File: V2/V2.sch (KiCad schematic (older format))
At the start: 197 parts

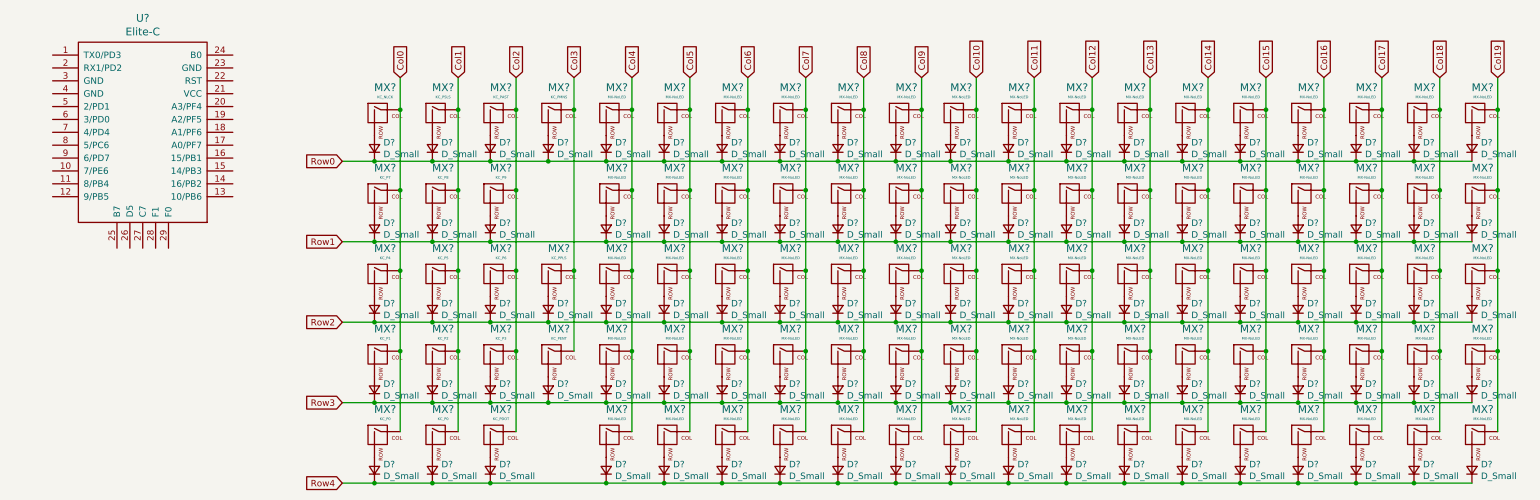
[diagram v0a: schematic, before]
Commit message: Assigned Footprints
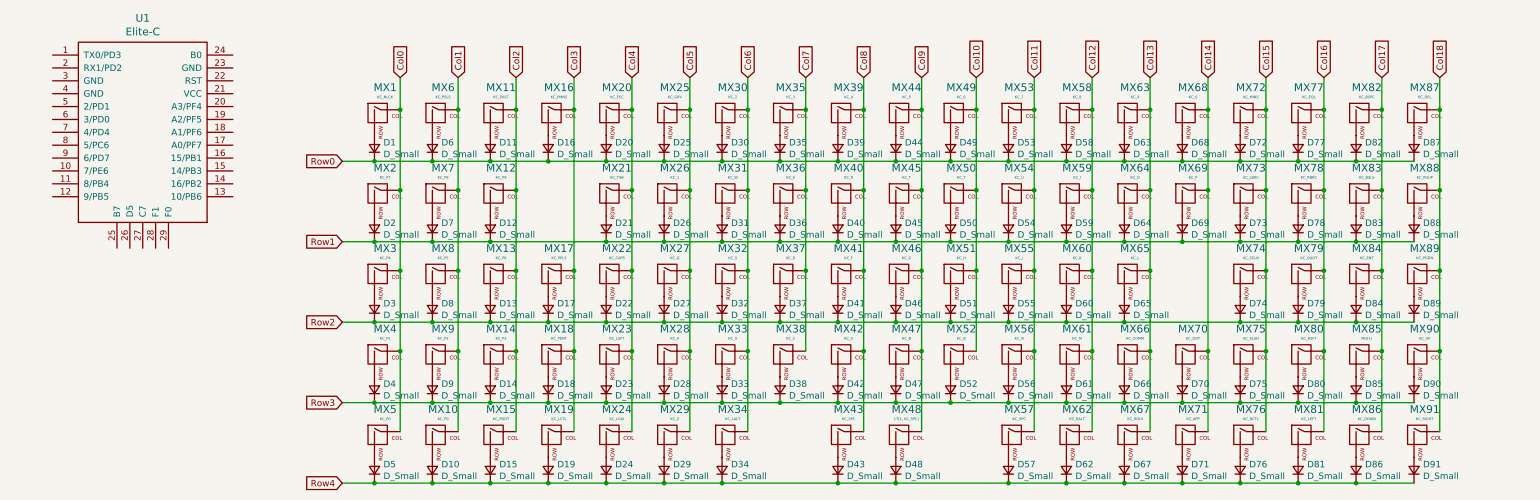
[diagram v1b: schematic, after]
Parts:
- removed D? (x8): D_Small, symbol Device:D_Small
- removed MX? (x8): MX-NoLED, symbol MX_Alps_Hybrid:MX-NoLED
- added D19: D_Small, Diode_SMD:D_SOD-123, symbol Device:D_Small
- added MX19: KC_LCTL, MX_Alps_Hybrid:MXOnly-1.25U-Hotswap, symbol MX_Alps_Hybrid:MX-NoLED
- D1, D10, D11, D12, D13, D14, D15, D16, D17, D18, D2, D20, D21, D22, D23, D24, D25, D26, D27, D28, D29, D3, D30, D31, D32, D33, D34, D35, D36, D37, D38, D39, D4, D40, D41, D42, D43, D44, D45, D46, D47, D48, D49, D5, D50, D51, D52, D53, D54, D55, D56, D57, D58, D59, D6, D60, D61, D62, D63, D64, D65, D66, D67, D68, D69, D7, D70, D71, D72, D73, D74, D75, D76, D77, D78, D79, D8, D80, D81, D82, D83, D84, D85, D86, D87, D88, D89, D9, D90, D91: renamed from D?; footprint (none) -> Diode_SMD:D_SOD-123
- MX1, MX10, MX11, MX12, MX13, MX14, MX15, MX16, MX2, MX3, MX4, MX5, MX6, MX7, MX8, MX9: renamed from MX?; footprint (none) -> MX_Alps_Hybrid:MXOnly-1U-Hotswap
- MX17, MX18: renamed from MX?; footprint (none) -> MX_Alps_Hybrid:MXOnly-2U-Hotswap
- MX20: renamed from MX?; value MX-NoLED -> KC_ESC; footprint (none) -> MX_Alps_Hybrid:MXOnly-1U-Hotswap
- MX21: renamed from MX?; value MX-NoLED -> KC_TAB; footprint (none) -> MX_Alps_Hybrid:MXOnly-1.5U-Hotswap
- MX22: renamed from MX?; value MX-NoLED -> KC_CAPS; footprint (none) -> MX_Alps_Hybrid:MXOnly-1.75U-Hotswap
- MX23: renamed from MX?; value MX-NoLED -> KC_LSFT; footprint (none) -> MX_Alps_Hybrid:MXOnly-2.25U-Hotswap
- MX24: renamed from MX?; value MX-NoLED -> KC_LGUI; footprint (none) -> MX_Alps_Hybrid:MXOnly-1.25U-Hotswap
- MX25: renamed from MX?; value MX-NoLED -> KC_GRV; footprint (none) -> MX_Alps_Hybrid:MXOnly-1U-Hotswap
- MX26: renamed from MX?; value MX-NoLED -> KC_1; footprint (none) -> MX_Alps_Hybrid:MXOnly-1U-Hotswap
- MX27: renamed from MX?; value MX-NoLED -> KC_Q; footprint (none) -> MX_Alps_Hybrid:MXOnly-1U-Hotswap
- MX28: renamed from MX?; value MX-NoLED -> KC_A; footprint (none) -> MX_Alps_Hybrid:MXOnly-1U-Hotswap
- MX29: renamed from MX?; value MX-NoLED -> KC_Z; footprint (none) -> MX_Alps_Hybrid:MXOnly-1U-Hotswap
- MX30: renamed from MX?; value MX-NoLED -> KC_2; footprint (none) -> MX_Alps_Hybrid:MXOnly-1U-Hotswap
- MX31: renamed from MX?; value MX-NoLED -> KC_W; footprint (none) -> MX_Alps_Hybrid:MXOnly-1U-Hotswap
- MX32: renamed from MX?; value MX-NoLED -> KC_S; footprint (none) -> MX_Alps_Hybrid:MXOnly-1U-Hotswap
- MX33: renamed from MX?; value MX-NoLED -> KC_X; footprint (none) -> MX_Alps_Hybrid:MXOnly-1U-Hotswap
- MX34: renamed from MX?; value MX-NoLED -> KC_LALT; footprint (none) -> MX_Alps_Hybrid:MXOnly-1.25U-Hotswap
- MX35: renamed from MX?; value MX-NoLED -> KC_3; footprint (none) -> MX_Alps_Hybrid:MXOnly-1U-Hotswap
- MX36: renamed from MX?; value MX-NoLED -> KC_E; footprint (none) -> MX_Alps_Hybrid:MXOnly-1U-Hotswap
- MX37: renamed from MX?; value MX-NoLED -> KC_D; footprint (none) -> MX_Alps_Hybrid:MXOnly-1U-Hotswap
- MX38: renamed from MX?; value MX-NoLED -> KC_C; footprint (none) -> MX_Alps_Hybrid:MXOnly-1U-Hotswap
- MX39: renamed from MX?; value MX-NoLED -> KC_4; footprint (none) -> MX_Alps_Hybrid:MXOnly-1U-Hotswap
- MX40: renamed from MX?; value MX-NoLED -> KC_R; footprint (none) -> MX_Alps_Hybrid:MXOnly-1U-Hotswap
- MX41: renamed from MX?; value MX-NoLED -> KC_F; footprint (none) -> MX_Alps_Hybrid:MXOnly-1U-Hotswap
- MX42: renamed from MX?; value MX-NoLED -> KC_V; footprint (none) -> MX_Alps_Hybrid:MXOnly-1U-Hotswap
- MX43: renamed from MX?; value MX-NoLED -> KC_SPC; footprint (none) -> MX_Alps_Hybrid:MXOnly-2.25U-Hotswap-ReversedStabilizers
- MX44: renamed from MX?; value MX-NoLED -> KC_5; footprint (none) -> MX_Alps_Hybrid:MXOnly-1U-Hotswap
- MX45: renamed from MX?; value MX-NoLED -> KC_T; footprint (none) -> MX_Alps_Hybrid:MXOnly-1U-Hotswap
- MX46: renamed from MX?; value MX-NoLED -> KC_G; footprint (none) -> MX_Alps_Hybrid:MXOnly-1U-Hotswap
- MX47, MX52: renamed from MX?; value MX-NoLED -> KC_B; footprint (none) -> MX_Alps_Hybrid:MXOnly-1U-Hotswap
- MX48: renamed from MX?; value MX-NoLED -> LT(1, KC_SPC); footprint (none) -> MX_Alps_Hybrid:MXOnly-1U-Hotswap
- MX49: renamed from MX?; value MX-NoLED -> KC_6; footprint (none) -> MX_Alps_Hybrid:MXOnly-1U-Hotswap
- MX50: renamed from MX?; value MX-NoLED -> KC_Y; footprint (none) -> MX_Alps_Hybrid:MXOnly-1U-Hotswap
- MX51: renamed from MX?; value MX-NoLED -> KC_H; footprint (none) -> MX_Alps_Hybrid:MXOnly-1U-Hotswap
- MX53: renamed from MX?; value MX-NoLED -> KC_7; footprint (none) -> MX_Alps_Hybrid:MXOnly-1U-Hotswap
- MX54: renamed from MX?; value MX-NoLED -> KC_U; footprint (none) -> MX_Alps_Hybrid:MXOnly-1U-Hotswap
- MX55: renamed from MX?; value MX-NoLED -> KC_J; footprint (none) -> MX_Alps_Hybrid:MXOnly-1U-Hotswap
- MX56: renamed from MX?; value MX-NoLED -> KC_N; footprint (none) -> MX_Alps_Hybrid:MXOnly-1U-Hotswap
- MX57: renamed from MX?; value MX-NoLED -> KC_SPC; footprint (none) -> MX_Alps_Hybrid:MXOnly-2.75U-Hotswap-ReversedStabilizers
- MX58: renamed from MX?; value MX-NoLED -> KC_8; footprint (none) -> MX_Alps_Hybrid:MXOnly-1U-Hotswap
- MX59: renamed from MX?; value MX-NoLED -> KC_I; footprint (none) -> MX_Alps_Hybrid:MXOnly-1U-Hotswap
- MX60: renamed from MX?; value MX-NoLED -> KC_K; footprint (none) -> MX_Alps_Hybrid:MXOnly-1U-Hotswap
- MX61: renamed from MX?; value MX-NoLED -> KC_M; footprint (none) -> MX_Alps_Hybrid:MXOnly-1U-Hotswap
- MX62: renamed from MX?; value MX-NoLED -> KC_RALT; footprint (none) -> MX_Alps_Hybrid:MXOnly-1.25U-Hotswap
- MX63: renamed from MX?; value MX-NoLED -> KC_9; footprint (none) -> MX_Alps_Hybrid:MXOnly-1U-Hotswap
- MX64: renamed from MX?; value MX-NoLED -> KC_O; footprint (none) -> MX_Alps_Hybrid:MXOnly-1U-Hotswap
- MX65: renamed from MX?; value MX-NoLED -> KC_L; footprint (none) -> MX_Alps_Hybrid:MXOnly-1U-Hotswap
- MX66: renamed from MX?; value MX-NoLED -> KC_COMM; footprint (none) -> MX_Alps_Hybrid:MXOnly-1U-Hotswap
- MX67: renamed from MX?; value MX-NoLED -> KC_RGUI; footprint (none) -> MX_Alps_Hybrid:MXOnly-1.25U-Hotswap
- MX68: renamed from MX?; value MX-NoLED -> KC_0; footprint (none) -> MX_Alps_Hybrid:MXOnly-1U-Hotswap
- MX69: renamed from MX?; value MX-NoLED -> KC_P; footprint (none) -> MX_Alps_Hybrid:MXOnly-1U-Hotswap
- MX70: renamed from MX?; value MX-NoLED -> KC_DOT; footprint (none) -> MX_Alps_Hybrid:MXOnly-1U-Hotswap
- MX71: renamed from MX?; value MX-NoLED -> KC_APP; footprint (none) -> MX_Alps_Hybrid:MXOnly-1.25U-Hotswap
- MX72: renamed from MX?; value MX-NoLED -> KC_MINS; footprint (none) -> MX_Alps_Hybrid:MXOnly-1U-Hotswap
- MX73: renamed from MX?; value MX-NoLED -> KC_LBRC; footprint (none) -> MX_Alps_Hybrid:MXOnly-1U-Hotswap
- MX74: renamed from MX?; value MX-NoLED -> KC_SCLN; footprint (none) -> MX_Alps_Hybrid:MXOnly-1U-Hotswap
- MX75: renamed from MX?; value MX-NoLED -> KC_SLSH; footprint (none) -> MX_Alps_Hybrid:MXOnly-1U-Hotswap
- MX76: renamed from MX?; value MX-NoLED -> KC_RCTL; footprint (none) -> MX_Alps_Hybrid:MXOnly-1.25U-Hotswap
- MX77: renamed from MX?; value MX-NoLED -> KC_EQL; footprint (none) -> MX_Alps_Hybrid:MXOnly-1U-Hotswap
- MX78: renamed from MX?; value MX-NoLED -> KC_RBRC; footprint (none) -> MX_Alps_Hybrid:MXOnly-1U-Hotswap
- MX79: renamed from MX?; value MX-NoLED -> KC_QUOT; footprint (none) -> MX_Alps_Hybrid:MXOnly-1U-Hotswap
- MX80: renamed from MX?; value MX-NoLED -> KC_RSFT; footprint (none) -> MX_Alps_Hybrid:MXOnly-1.75U-Hotswap
- MX81: renamed from MX?; value MX-NoLED -> KC_LEFT; footprint (none) -> MX_Alps_Hybrid:MXOnly-1U-Hotswap
- MX82: renamed from MX?; value MX-NoLED -> KC_BSPC; footprint (none) -> MX_Alps_Hybrid:MXOnly-2U-Hotswap
- MX83: renamed from MX?; value MX-NoLED -> KC_BSLS; footprint (none) -> MX_Alps_Hybrid:MXOnly-1.5U-Hotswap
- MX84: renamed from MX?; value MX-NoLED -> KC_ENT; footprint (none) -> MX_Alps_Hybrid:MXOnly-2.25U-Hotswap
- MX85: renamed from MX?; value MX-NoLED -> MO(1); footprint (none) -> MX_Alps_Hybrid:MXOnly-1U-Hotswap
- MX86: renamed from MX?; value MX-NoLED -> KC_DOWN; footprint (none) -> MX_Alps_Hybrid:MXOnly-1U-Hotswap
- MX87: renamed from MX?; value MX-NoLED -> KC_DEL; footprint (none) -> MX_Alps_Hybrid:MXOnly-1U-Hotswap
- MX88: renamed from MX?; value MX-NoLED -> KC_PGUP; footprint (none) -> MX_Alps_Hybrid:MXOnly-1U-Hotswap
- MX89: renamed from MX?; value MX-NoLED -> KC_PGDN; footprint (none) -> MX_Alps_Hybrid:MXOnly-1U-Hotswap
- MX90: renamed from MX?; value MX-NoLED -> KC_UP; footprint (none) -> MX_Alps_Hybrid:MXOnly-1U-Hotswap
- MX91: renamed from MX?; value MX-NoLED -> KC_RIGHT; footprint (none) -> MX_Alps_Hybrid:MXOnly-1U-Hotswap
- U1: renamed from U?; footprint (none) -> Keebio-Parts:Elite-C-castellated-29pin-holes
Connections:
- net Col3: now also MX19.1 (COL)
- net Row4: now also D19.1 (K)
- new net: D19.2 (A), MX19.2 (ROW)

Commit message: Updated schematic and pcb design
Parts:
- added MX92: KC_P0, MX_Alps_Hybrid:MXOnly-2U-Hotswap-ReversedStabilizers, symbol MX_Alps_Hybrid:MX-NoLED
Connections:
- net Col0: now also MX92.1 (COL)
- net at D5.2 (A), MX5.2 (ROW): now also MX92.2 (ROW)
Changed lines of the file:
@@
 Wire Wire Line
 	9075 2900 9975 2900
+$Comp
+L MX_Alps_Hybrid:MX-NoLED MX92
+U 1 1 60EC3BEF
+P 3275 3775
+F 0 "MX92" H 3308 3998 60  0000 C CNN
+F 1 "KC_P0" H 3308 3924 20  0000 C CNN
+F 2 "MX_Alps_Hybrid:MXOnly-2U-Hotswap-ReversedStabilizers" H 2650 3750 60  0001 C CNN
+F 3 "" H 2650 3750 60  0001 C CNN
+	1    3275 3775
+	1    0    0    -1
+$EndComp
+Wire Wire Line
+	3425 3725 3425 3750
+Wire Wire Line
+	3425 3750 3450 3750
+Connection ~ 3450 3750
+Wire Wire Line
+	3225 3925 3225 3950
+Wire Wire Line
+	3225 3950 3250 3950
+Connection ~ 3250 3950
 $EndSCHEMATC

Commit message: Finished PCB
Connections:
- net Col0: now also U1.1 (TX0/PD3)
- net Col1: now also U1.2 (RX1/PD2)
- net Col10: now also U1.13 (10/PB6)
- net Col11: now also U1.14 (16/PB2)
- net Col12: now also U1.15 (14/PB3)
- net Col13: now also U1.16 (15/PB1)
- net Col14: now also U1.17 (A0/PF7)
- net Col15: now also U1.18 (A1/PF6)
- net Col16: now also U1.19 (A2/PF5)
- net Col17: now also U1.20 (A3/PF4)
- net Col18: now also U1.24 (B0)
- net Col2: now also U1.5 (2/PD1)
- net Col3: now also U1.6 (3/PD0)
- net Col4: now also U1.7 (4/PD4)
- net Col5: now also U1.8 (5/PC6)
- net Col6: now also U1.9 (6/PD7)
- net Col7: now also U1.10 (7/PE6)
- net Col8: now also U1.11 (8/PB4)
- net Col9: now also U1.12 (9/PB5)
- net Row0: now also U1.25 (B7)
- net Row1: now also U1.26 (D5)
- net Row2: now also U1.28 (F1)
- net Row3: now also U1.29 (F0)
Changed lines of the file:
@@
 	3225 3950 3250 3950
 Connection ~ 3250 3950
+Text GLabel 750  825  0    50   Input ~ 0
+Col0
+Text GLabel 750  925  0    50   Input ~ 0
+Col1
+Text GLabel 750  1225 0    50   Input ~ 0
+Col2
+Text GLabel 750  1325 0    50   Input ~ 0
+Col3
+Text GLabel 750  1425 0    50   Input ~ 0
+Col4
+Text GLabel 750  1525 0    50   Input ~ 0
+Col5
+Text GLabel 750  1725 0    50   Input ~ 0
+Col7
+Text GLabel 750  1825 0    50   Input ~ 0
+Col8
+Text GLabel 750  1925 0    50   Input ~ 0
+Col9
+Text GLabel 750  1625 0    50   Input ~ 0
+Col6
+Text GLabel 1250 2325 3    50   Input ~ 0
+Row0
+Text GLabel 1350 2325 3    50   Input ~ 0
+Row1
+Text GLabel 1550 2325 3    50   Input ~ 0
+Row2
+Text GLabel 1650 2325 3    50   Input ~ 0
+Row3
+Text GLabel 2150 825  2    50   Input ~ 0
+Col18
+Text GLabel 2150 1225 2    50   Input ~ 0
+Col17
+Text GLabel 2150 1325 2    50   Input ~ 0
+Col16
+Text GLabel 2150 1425 2    50   Input ~ 0
+Col15
+Text GLabel 2150 1525 2    50   Input ~ 0
+Col14
+Text GLabel 2150 1625 2    50   Input ~ 0
+Col13
+Text GLabel 2150 1725 2    50   Input ~ 0
+Col12
+Text GLabel 2150 1825 2    50   Input ~ 0
+Col11
+Text GLabel 2150 1925 2    50   Input ~ 0
+Col10
 $EndSCHEMATC

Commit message: Error Fixed
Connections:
- net Row4: now also U1.27 (C7)
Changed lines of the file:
@@
 Text GLabel 2150 1925 2    50   Input ~ 0
 Col10
+Text GLabel 1450 2325 3    50   Input ~ 0
+Row4
 $EndSCHEMATC
